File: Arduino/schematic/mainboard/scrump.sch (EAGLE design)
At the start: 26 parts, among them J1 PINHEAD-FTSH, J2 USB-CON-5PIN-105017-0001, U1 ATSAMD21G-A, U2 LM3671, U3 MCP73831, Y1 32.768kHz

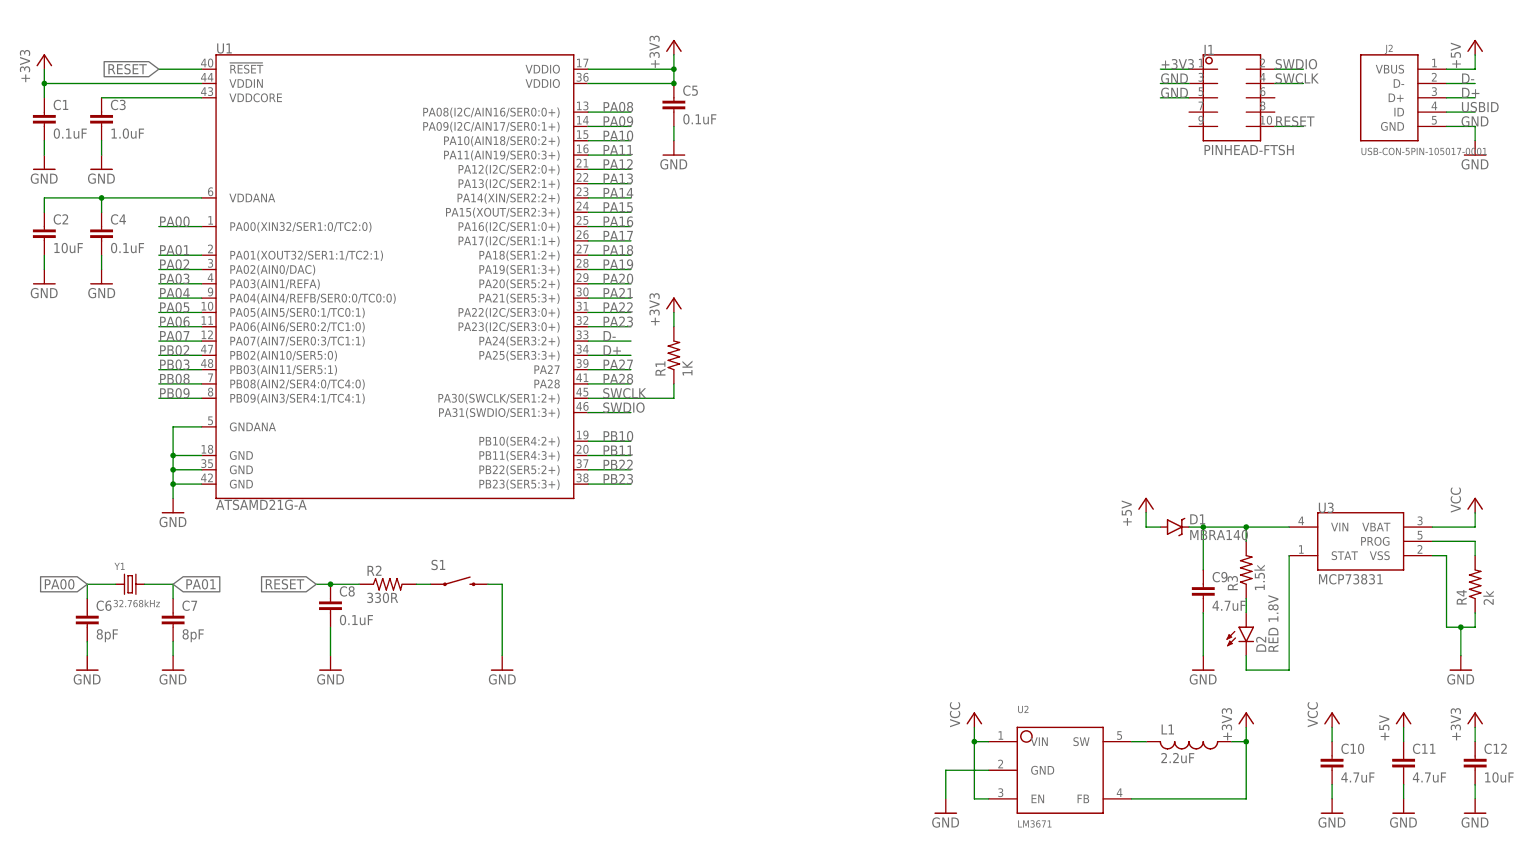
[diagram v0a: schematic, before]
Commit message: Fixed issues after review - Missing 3.3V line on Vddana - Added decoupling cap for second vddio - Removed pull-up on swdclk, which is usually included in the programmer itself. - Added 22 ohm resistor in series with D+ and D-(USB) - Pin 9 of the SWD header is also GND
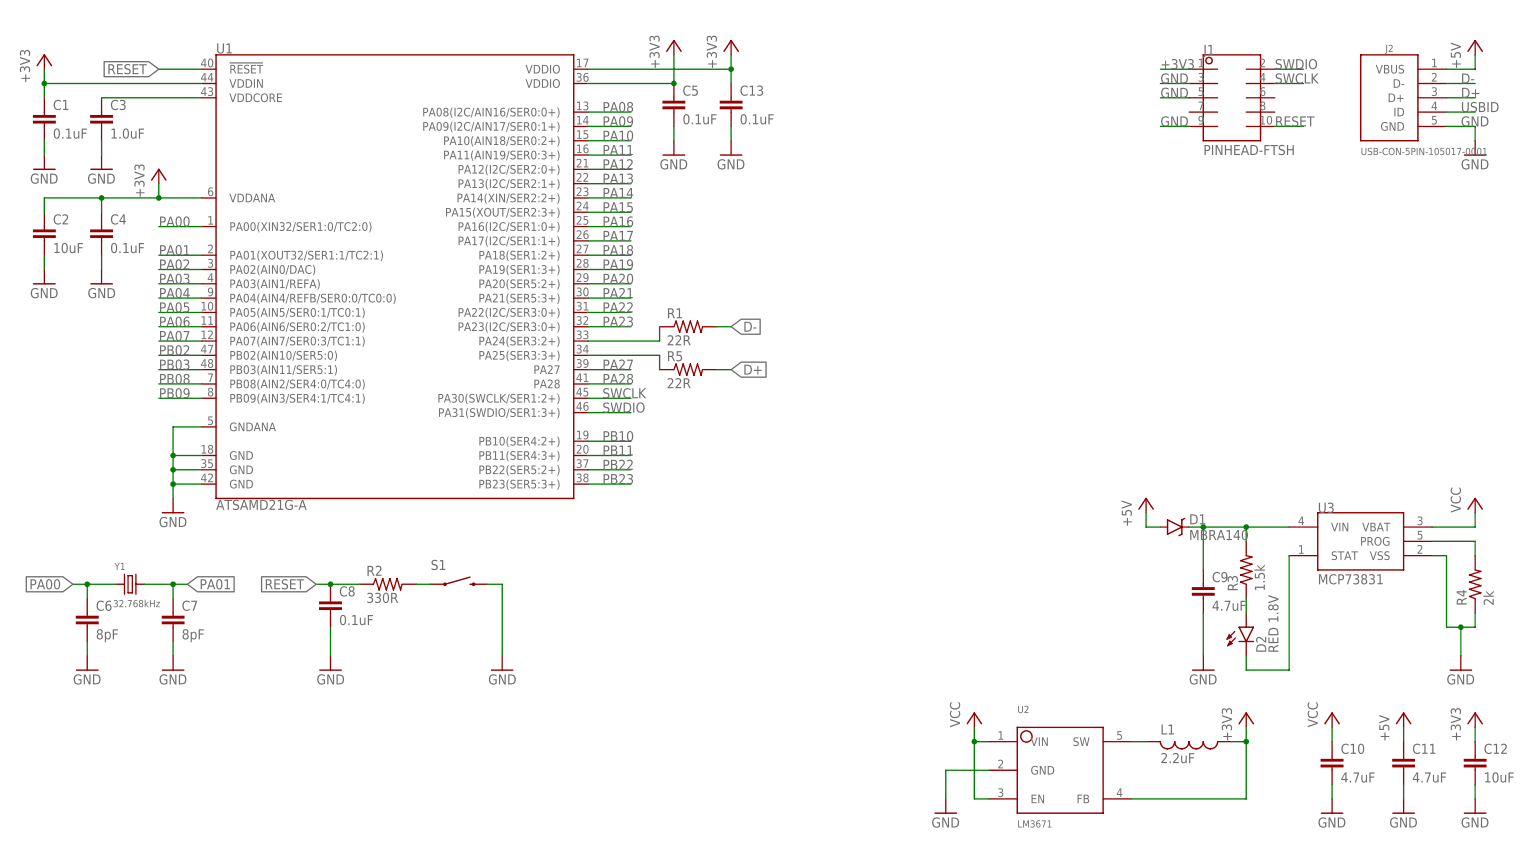
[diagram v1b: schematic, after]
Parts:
- added C13: 0.1uF, SparkFun-Capacitors:CAP0603-CAP
- added R5: 22R, SparkFun-Resistors:RESISTOR0603
- R1: value 1K -> 22R
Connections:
- new net N$9: R1.1, U1.PA24(SER3:2+)
- net +3V3: now also C13.1, C2.1, C4.1, U1.VDDANA; no longer R1.2
- net D+: now also R5.2; no longer U1.PA25(SER3:3+)
- net D-: now also R1.2; no longer U1.PA24(SER3:2+)
- net GND: now also C13.2, J1.P$9
- net N$4: now also R5.1, U1.PA25(SER3:3+); no longer C2.1, C4.1, U1.VDDANA
- net SWCLK: no longer R1.1
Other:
- moved on the sheet: R1
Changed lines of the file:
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@@
 <part name="GND4" library="supply1" deviceset="GND" device=""/>
 <part name="GND2" library="supply1" deviceset="GND" device=""/>
-<part name="+3V33" library="supply1" deviceset="+3V3" device=""/>
 <part name="+3V32" library="supply1" deviceset="+3V3" device=""/>
 <part name="+3V31" library="supply1" deviceset="+3V3" device=""/>
@@
 <part name="C3" library="SparkFun-Capacitors" deviceset="CAP" device="0603-CAP" value="1.0uF"/>
 <part name="C1" library="SparkFun-Capacitors" deviceset="CAP" device="0603-CAP" value="0.1uF"/>
-<part name="R1" library="SparkFun-Resistors" deviceset="RESISTOR" device="0603" value="1K"/>
 <part name="FRAME1" library="SparkFun-Aesthetics" deviceset="FRAME-A4L" device=""/>
 <part name="J2" library="mylibrary" deviceset="USB-CON-5PIN" device="-105017-0001"/>
@@
 <part name="P+3" library="supply1" deviceset="VCC" device=""/>
 <part name="D2" library="SparkFun-LED" deviceset="LED-RED" device="0603" value="RED 1.8V"/>
+<part name="+3V1" library="supply1" deviceset="+3V3" device=""/>
+<part name="C13" library="SparkFun-Capacitors" deviceset="CAP" device="0603-CAP" value="0.1uF"/>
+<part name="GND18" library="supply1" deviceset="GND" device=""/>
+<part name="+3V2" library="supply1" deviceset="+3V3" device=""/>
+<part name="R1" library="SparkFun-Resistors" deviceset="RESISTOR" device="0603" value="22R"/>
+<part name="R5" library="SparkFun-Resistors" deviceset="RESISTOR" device="0603" value="22R"/>
 </parts>
 <sheets>
@@
 <instance part="GND4" gate="1" x="22.86" y="132.08" rot="MR0"/>
 <instance part="GND2" gate="1" x="12.7" y="132.08"/>
-<instance part="+3V33" gate="G$1" x="124.46" y="129.54"/>
 <instance part="+3V32" gate="G$1" x="124.46" y="175.26"/>
 <instance part="+3V31" gate="G$1" x="12.7" y="172.72"/>
@@
 <instance part="C3" gate="G$1" x="22.86" y="160.02"/>
 <instance part="C1" gate="G$1" x="12.7" y="160.02"/>
-<instance part="R1" gate="G$1" x="124.46" y="119.38" rot="R90"/>
 <instance part="FRAME1" gate="G$1" x="2.54" y="2.54" smashed="yes">
 <attribute name="DRAWING_NAME" x="184.15" y="13.97" size="2.54" layer="94" font="vector"/>
@@
 <instance part="P+3" gate="VCC" x="241.3" y="55.88"/>
 <instance part="D2" gate="G$1" x="226.06" y="71.12"/>
+<instance part="+3V1" gate="G$1" x="33.02" y="152.4"/>
+<instance part="C13" gate="G$1" x="134.62" y="162.56"/>
+<instance part="GND18" gate="1" x="134.62" y="154.94"/>
+<instance part="+3V2" gate="G$1" x="134.62" y="175.26"/>
+<instance part="R1" gate="G$1" x="127" y="124.46"/>
+<instance part="R5" gate="G$1" x="127" y="116.84"/>
 </instances>
 <busses>
@@
 <junction x="264.16" y="71.12"/>
 </segment>
-</net>
-<net name="N$4" class="0">
-<segment>
-<pinref part="U1" gate="G$1" pin="VDDANA"/>
-<wire x1="40.64" y1="147.32" x2="22.86" y2="147.32" width="0.1524" layer="91"/>
-<wire x1="22.86" y1="147.32" x2="22.86" y2="144.78" width="0.1524" layer="91"/>
-<wire x1="12.7" y1="144.78" x2="12.7" y2="147.32" width="0.1524" layer="91"/>
-<wire x1="12.7" y1="147.32" x2="22.86" y2="147.32" width="0.1524" layer="91"/>
-<junction x="22.86" y="147.32"/>
-<pinref part="C4" gate="G$1" pin="1"/>
-<pinref part="C2" gate="G$1" pin="1"/>
+<segment>
+<pinref part="GND18" gate="1" pin="GND"/>
+<pinref part="C13" gate="G$1" pin="2"/>
+<wire x1="134.62" y1="157.48" x2="134.62" y2="160.02" width="0.1524" layer="91"/>
+</segment>
+<segment>
+<pinref part="J1" gate="G$1" pin="P$9"/>
+<wire x1="215.9" y1="160.02" x2="210.82" y2="160.02" width="0.1524" layer="91"/>
+<label x="210.82" y="160.02" size="1.778" layer="95"/>
 </segment>
 </net>
@@
 <net name="+3V3" class="0">
 <segment>
-<pinref part="+3V33" gate="G$1" pin="+3V3"/>
-<wire x1="124.46" y1="127" x2="124.46" y2="124.46" width="0.1524" layer="91"/>
-<pinref part="R1" gate="G$1" pin="2"/>
-</segment>
-<segment>
 <pinref part="U1" gate="G$1" pin="VDDIO@17"/>
-<wire x1="109.22" y1="170.18" x2="124.46" y2="170.18" width="0.1524" layer="91"/>
-<wire x1="124.46" y1="170.18" x2="124.46" y2="167.64" width="0.1524" layer="91"/>
-<pinref part="U1" gate="G$1" pin="VDDIO@36"/>
-<wire x1="109.22" y1="167.64" x2="124.46" y2="167.64" width="0.1524" layer="91"/>
-<pinref part="+3V32" gate="G$1" pin="+3V3"/>
-<wire x1="124.46" y1="170.18" x2="124.46" y2="172.72" width="0.1524" layer="91"/>
-<junction x="124.46" y="170.18"/>
-<pinref part="C5" gate="G$1" pin="1"/>
-<junction x="124.46" y="167.64"/>
+<wire x1="109.22" y1="170.18" x2="134.62" y2="170.18" width="0.1524" layer="91"/>
+<pinref part="C13" gate="G$1" pin="1"/>
+<wire x1="134.62" y1="167.64" x2="134.62" y2="170.18" width="0.1524" layer="91"/>
+<pinref part="+3V2" gate="G$1" pin="+3V3"/>
+<wire x1="134.62" y1="170.18" x2="134.62" y2="172.72" width="0.1524" layer="91"/>
+<junction x="134.62" y="170.18"/>
 </segment>
 <segment>
@@
 <junction x="226.06" y="50.8"/>
 </segment>
+<segment>
+<pinref part="U1" gate="G$1" pin="VDDANA"/>
+<wire x1="40.64" y1="147.32" x2="33.02" y2="147.32" width="0.1524" layer="91"/>
+<wire x1="33.02" y1="147.32" x2="22.86" y2="147.32" width="0.1524" layer="91"/>
+<wire x1="22.86" y1="147.32" x2="22.86" y2="144.78" width="0.1524" layer="91"/>
+<junction x="22.86" y="147.32"/>
+<pinref part="C4" gate="G$1" pin="1"/>
+<pinref part="C2" gate="G$1" pin="1"/>
+<wire x1="12.7" y1="147.32" x2="22.86" y2="147.32" width="0.1524" layer="91"/>
+<wire x1="12.7" y1="144.78" x2="12.7" y2="147.32" width="0.1524" layer="91"/>
+<pinref part="+3V1" gate="G$1" pin="+3V3"/>
+<wire x1="33.02" y1="149.86" x2="33.02" y2="147.32" width="0.1524" layer="91"/>
+<junction x="33.02" y="147.32"/>
+</segment>
+<segment>
+<pinref part="C5" gate="G$1" pin="1"/>
+<pinref part="U1" gate="G$1" pin="VDDIO@36"/>
+<wire x1="109.22" y1="167.64" x2="124.46" y2="167.64" width="0.1524" layer="91"/>
+<pinref part="+3V32" gate="G$1" pin="+3V3"/>
+<wire x1="124.46" y1="172.72" x2="124.46" y2="167.64" width="0.1524" layer="91"/>
+<junction x="124.46" y="167.64"/>
+</segment>
 </net>
 <net name="SWCLK" class="0">
 <segment>
 <pinref part="U1" gate="G$1" pin="PA30(SWCLK/SER1:2+)"/>
-<wire x1="124.46" y1="114.3" x2="124.46" y2="111.76" width="0.1524" layer="91"/>
-<wire x1="124.46" y1="111.76" x2="109.22" y2="111.76" width="0.1524" layer="91"/>
+<wire x1="116.84" y1="111.76" x2="109.22" y2="111.76" width="0.1524" layer="91"/>
 <label x="111.76" y="111.76" size="1.778" layer="95"/>
-<pinref part="R1" gate="G$1" pin="1"/>
 </segment>
 <segment>
@@
 <pinref part="C6" gate="G$1" pin="1"/>
 <wire x1="20.32" y1="76.2" x2="20.32" y2="78.74" width="0.1524" layer="91"/>
-<label x="20.32" y="78.74" size="1.778" layer="95" font="vector" rot="R180" xref="yes"/>
+<wire x1="20.32" y1="78.74" x2="17.78" y2="78.74" width="0.1524" layer="91"/>
+<junction x="20.32" y="78.74"/>
+<label x="17.78" y="78.74" size="1.778" layer="95" rot="R180" xref="yes"/>
 </segment>
 </net>
@@
 <pinref part="C7" gate="G$1" pin="1"/>
 <wire x1="35.56" y1="76.2" x2="35.56" y2="78.74" width="0.1524" layer="91"/>
-<label x="35.56" y="78.74" size="1.778" layer="95" font="vector" xref="yes"/>
+<wire x1="35.56" y1="78.74" x2="38.1" y2="78.74" width="0.1524" layer="91"/>
+<junction x="35.56" y="78.74"/>
+<label x="38.1" y="78.74" size="1.778" layer="95" xref="yes"/>
 </segment>
 </net>
@@
 </segment>
 <segment>
-<pinref part="U1" gate="G$1" pin="PA25(SER3:3+)"/>
-<wire x1="109.22" y1="119.38" x2="116.84" y2="119.38" width="0.1524" layer="91"/>
-<label x="111.76" y="119.38" size="1.778" layer="95"/>
+<pinref part="R5" gate="G$1" pin="2"/>
+<wire x1="132.08" y1="116.84" x2="134.62" y2="116.84" width="0.1524" layer="91"/>
+<label x="134.62" y="116.84" size="1.778" layer="95" xref="yes"/>
 </segment>
 </net>
@@
 </segment>
 <segment>
-<pinref part="U1" gate="G$1" pin="PA24(SER3:2+)"/>
-<wire x1="109.22" y1="121.92" x2="116.84" y2="121.92" width="0.1524" layer="91"/>
-<label x="111.76" y="121.92" size="1.778" layer="95"/>
+<pinref part="R1" gate="G$1" pin="2"/>
+<wire x1="132.08" y1="124.46" x2="134.62" y2="124.46" width="0.1524" layer="91"/>
+<label x="134.62" y="124.46" size="1.778" layer="95" xref="yes"/>
 </segment>
 </net>
@@
 </segment>
 </net>
+<net name="N$4" class="0">
+<segment>
+<pinref part="U1" gate="G$1" pin="PA25(SER3:3+)"/>
+<pinref part="R5" gate="G$1" pin="1"/>
+<wire x1="109.22" y1="119.38" x2="121.92" y2="119.38" width="0.1524" layer="91"/>
+<wire x1="121.92" y1="119.38" x2="121.92" y2="116.84" width="0.1524" layer="91"/>
+</segment>
+</net>
+<net name="N$9" class="0">
+<segment>
+<pinref part="R1" gate="G$1" pin="1"/>
+<pinref part="U1" gate="G$1" pin="PA24(SER3:2+)"/>
+<wire x1="121.92" y1="124.46" x2="121.92" y2="121.92" width="0.1524" layer="91"/>
+<wire x1="121.92" y1="121.92" x2="109.22" y2="121.92" width="0.1524" layer="91"/>
+</segment>
+</net>

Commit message: Added DHT11
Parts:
- added B1: BMP180BREAKOUT, mylibrary:BMP180BREAKOUT
- C6, C7: value 8pF -> 22pF
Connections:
- removed net PA22: U1.PA22(I2C/SER3:0+)
- removed net PA23: U1.PA23(I2C/SER3:0+)
- new net SCL: B1.SCL, U1.PA23(I2C/SER3:0+)
- new net SDA: B1.SDA, U1.PA22(I2C/SER3:0+)
- net +3V3: now also B1.3V3
- net D+: now also U1.PA25(SER3:3+); no longer J2.D+
- net D-: now also U1.PA24(SER3:2+); no longer J2.D-
- net GND: now also B1.GND
- net N$4: now also J2.D+; no longer U1.PA25(SER3:3+)
- net N$9: now also J2.D-; no longer U1.PA24(SER3:2+)
